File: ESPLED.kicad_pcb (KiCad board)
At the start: 2 copper layers, 81.3 x 83.8 mm, 24 parts, among them CON1 BARREL_JACK, J1 USB_B_Micro, P2 LED_CON, P3 LED_CON_SCREW, P4 LED_CON_SCREW, Q1 IRLZ34N, Q2 IRLZ34N, Q3 IRLZ34N, SW1 Reset, SW2 Program, U1 LM1117-3.3, U2 ESP-07v2, U3 INTERFACE-CH340G, Y1 Crystal

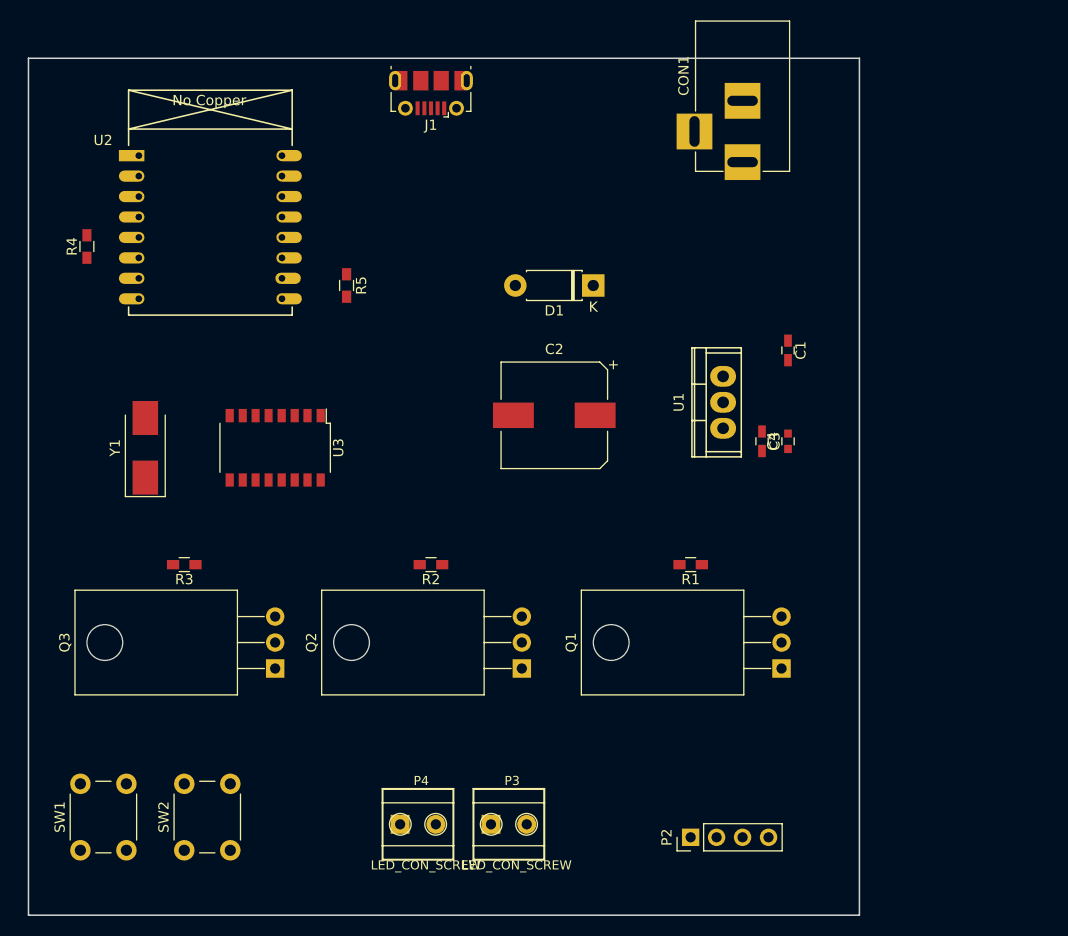
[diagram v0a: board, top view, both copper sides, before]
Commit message: Added caps for crystal
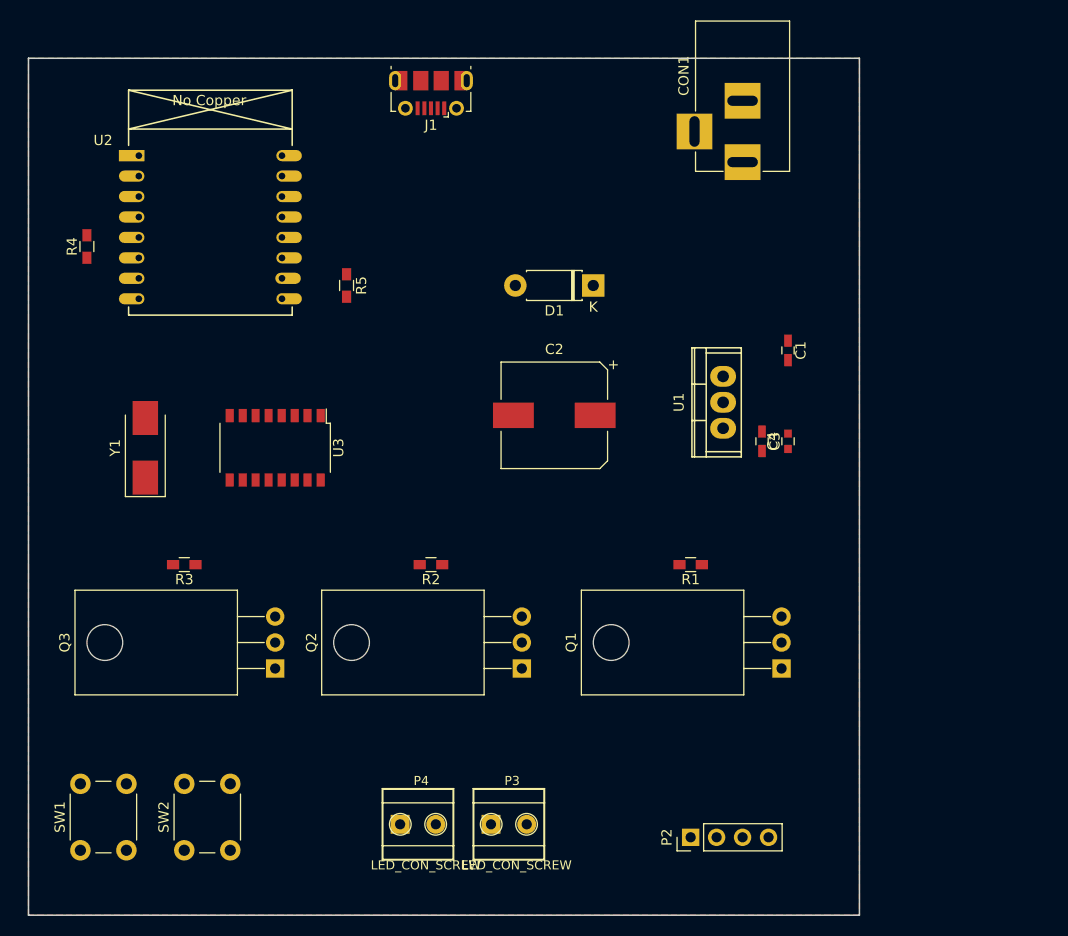
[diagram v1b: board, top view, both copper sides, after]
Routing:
- added copper zone on F.Cu, net GND
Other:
- net class High Power added: clearance 0.2, trace_width 0.25, via_dia 0.6, via_drill 0.4
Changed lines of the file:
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@@
     (links 62)
     (no_connects 60)
-    (area 0 0 0 0)
+    (area 92.634999 41.654999 174.065001 129.615001)
     (thickness 1.6)
-    (drawings 4)
+    (drawings 5)
     (tracks 0)
     (zones 0)
@@
     (add_net VUSB)
   )
+  (net_class "High Power" ""
+    (clearance 0.2)
+    (trace_width 0.25)
+    (via_dia 0.6)
+    (via_drill 0.4)
+    (uvia_dia 0.3)
+    (uvia_drill 0.1)
+  )
   (module Connectors:BARREL_JACK (layer F.Cu)
     (at 162.56 55.88 270)
@@
     )
   )
+  (dimension 83.82 (width 0.3) (layer Eco1.User)
+    (gr_text "83,820 mm" (at 189.31 87.63 270) (layer Eco1.User)
+      (effects (font (size 1.5 1.5) (thickness 0.3)))
+    )
+    (feature1 (pts (xy 179.07 129.54) (xy 190.66 129.54)))
+    (feature2 (pts (xy 179.07 45.72) (xy 190.66 45.72)))
+    (crossbar (pts (xy 187.96 45.72) (xy 187.96 129.54)))
+    (arrow1a (pts (xy 187.96 129.54) (xy 187.373579 128.413496)))
+    (arrow1b (pts (xy 187.96 129.54) (xy 188.546421 128.413496)))
+    (arrow2a (pts (xy 187.96 45.72) (xy 187.373579 46.846504)))
+    (arrow2b (pts (xy 187.96 45.72) (xy 188.546421 46.846504)))
+  )
   (gr_line (start 92.71 45.72) (end 173.99 45.72) (angle 90) (layer Edge.Cuts) (width 0.15))
   (gr_line (start 92.71 129.54) (end 92.71 45.72) (angle 90) (layer Edge.Cuts) (width 0.15))
   (gr_line (start 173.99 129.54) (end 92.71 129.54) (angle 90) (layer Edge.Cuts) (width 0.15))
   (gr_line (start 173.99 45.72) (end 173.99 129.54) (angle 90) (layer Edge.Cuts) (width 0.15))
+  (zone (net 2) (net_name GND) (layer F.Cu) (hatch edge 0.508)
+    (connect_pads (clearance 0.508))
+    (min_thickness 0.254)
+    (fill (arc_segments 16) (thermal_gap 0.508) (thermal_bridge_width 0.508))
+    (polygon
+      (pts
+        (xy 173.99 129.54) (xy 92.71 129.54) (xy 92.71 45.72) (xy 173.99 45.72)
+      )
+    )
+  )
 )

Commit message: Footprint research done, layout more or less gelayoutet
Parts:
- removed P4: LED_CON_SCREW, SeeedOPL-Connector:H2-3.5-7.0X7.0MM
- added C5: 22p, Capacitor_SMD:C_0603_1608Metric_Pad1.05x0.95mm_HandSolder, F.Cu at (112.9, 86.5)
- added C6: 22p, Capacitor_SMD:C_0603_1608Metric_Pad1.05x0.95mm_HandSolder, F.Cu at (112.9, 78.5)
- added C7: 100n, Capacitor_SMD:C_0603_1608Metric_Pad1.05x0.95mm_HandSolder, F.Cu at (133.0, 86.0)
- added F1: Polyfuse, Fuse:Fuse_1812_4532Metric_Pad1.30x3.40mm_HandSolder, F.Cu at (103.0, 69.7)
- added J2: LED_CON_RGB, Connector_PinHeader_2.54mm:PinHeader_1x04_P2.54mm_Vertical, F.Cu at (190.0, 111.0)
- added J3: LED_CON_WW, Connector_PinHeader_2.54mm:PinHeader_1x02_P2.54mm_Vertical, F.Cu at (185.0, 106.0)
- added J4: MIC, Connector_PinHeader_2.54mm:PinHeader_1x03_P2.54mm_Vertical, F.Cu at (145.0, 83.0)
- added JP1: GPIO LINK, Jumper:SolderJumper-2_P1.3mm_Open_RoundedPad1.0x1.5mm, F.Cu at (144.6, 90.5)
- added JP2: GPIO LINK, Jumper:SolderJumper-2_P1.3mm_Open_RoundedPad1.0x1.5mm, F.Cu at (107.4, 90.8)
- added JP3: GPIO LINK, Jumper:SolderJumper-2_P1.3mm_Open_RoundedPad1.0x1.5mm, F.Cu at (132.2, 90.7)
- added JP4: GND LINK, Jumper:SolderJumper-2_P1.3mm_Open_TrianglePad1.0x1.5mm, F.Cu at (98.2, 90.8)
- added JP5: GPIO LINK, Jumper:SolderJumper-2_P1.3mm_Open_RoundedPad1.0x1.5mm, F.Cu at (119.8, 90.5)
- added JP6: GPIO LINK, Jumper:SolderJumper-2_P1.3mm_Open_RoundedPad1.0x1.5mm, F.Cu at (95.0, 90.8)
- added P1: LED_CON_SCREW, TerminalBlock:TerminalBlock_Altech_AK300-2_P5.00mm, F.Cu at (186.0, 74.0)
- added Q4: IRLZ34N, Package_TO_SOT_THT:TO-220-3_Horizontal_TabDown, F.Cu at (113.4, 94.4)
- added Q5: IRLZ34N, Package_TO_SOT_THT:TO-220-3_Horizontal_TabDown, F.Cu at (100.9, 94.5)
- added R6: 100, Resistor_SMD:R_0603_1608Metric_Pad1.05x0.95mm_HandSolder, F.Cu at (113.6, 90.8)
- added R7: 100, Resistor_SMD:R_0603_1608Metric_Pad1.05x0.95mm_HandSolder, F.Cu at (101.2, 90.8)
- added R8: 4.7K, Resistor_SMD:R_0603_1608Metric_Pad1.05x0.95mm_HandSolder, F.Cu at (132.0, 83.0)
- added SW3: Mode, Button_Switch_THT:SW_PUSH_6mm, F.Cu at (174.0, 113.0)
- added U4: DS18B20, Package_TO_SOT_THT:TO-92_HandSolder, F.Cu at (136.9, 81.8)
- C1, C3: footprint Capacitors_SMD:C_0603_HandSoldering -> Capacitor_SMD:C_0603_1608Metric_Pad1.05x0.95mm_HandSolder
- C2: footprint Capacitors_SMD:CP_Elec_10x10.5 -> Capacitor_SMD:CP_Elec_10x10.5
- C4: footprint Capacitors_SMD:C_0603 -> Capacitor_SMD:C_0603_1608Metric_Pad1.05x0.95mm_HandSolder
- CON1: footprint Connectors:BARREL_JACK -> Connector_BarrelJack:BarrelJack_Horizontal
- D1: value 1N5819 -> 1N5817; footprint Diode_THT:D_DO-41_SOD81_P7.62mm_Horizontal -> Diode_SMD:D_SMA_Handsoldering
- J1: footprint Connectors_USB:USB_Micro-B_Molex-105017-0001 -> Connector_USB:USB_Micro-B_Molex-105017-0001
- P2: value LED_CON -> LED_CON_SCREW; footprint Pin_Headers:Pin_Header_Straight_1x04_Pitch2.54mm -> TerminalBlock:TerminalBlock_Altech_AK300-2_P5.00mm
- P3: footprint SeeedOPL-Connector:H2-3.5-7.0X7.0MM -> TerminalBlock:TerminalBlock_Altech_AK300-2_P5.00mm
- Q1, Q2, Q3: footprint TO_SOT_Packages_THT:TO-220_Horizontal -> Package_TO_SOT_THT:TO-220-3_Horizontal_TabDown
- R1, R2, R3, R4, R5: footprint Resistors_SMD:R_0603_HandSoldering -> Resistor_SMD:R_0603_1608Metric_Pad1.05x0.95mm_HandSolder
- SW1: footprint Buttons_Switches_THT:SW_PUSH_6mm_h5mm -> Button_Switch_THT:SW_PUSH_6mm
- SW2: footprint Button_Switch_THT:SW_PUSH_6mm_H5mm -> Button_Switch_THT:SW_PUSH_6mm
- U1: value LM1117-3.3 -> AMS1117-3.3; footprint Power_Integrations:TO-220 -> Package_TO_SOT_SMD:SOT-223-3_TabPin2
- U2: footprint ESP8266:ESP-07v2 -> RF_Module:ESP-07
- U3: footprint Housings_SSOP:SOP-16_4.4x10.4mm_Pitch1.27mm -> Package_SO:SOIC-16W_5.3x10.2mm_P1.27mm
- moved U2 67.1 mm to (167.0, 77.0)
- moved CON1 61.4 mm to (107.0, 82.0), turned to 0 degrees
- moved SW1 59.1 mm to (156.0, 113.0)
- moved R4 59.0 mm to (156.0, 77.1)
- moved SW2 58.0 mm to (165.0, 113.0)
- moved R5 56.8 mm to (178.0, 85.0)
- moved C3 56.2 mm to (110.0, 69.2), turned to 90 degrees
- moved P3 51.6 mm to (186.0, 98.0), turned to 90 degrees
- moved P2 45.9 mm to (186.0, 86.0)
- moved U1 45.1 mm to (116.4, 71.0), turned to 0 degrees
- moved C1 44.0 mm to (123.0, 74.9)
- moved D1 42.5 mm to (106.0, 75.0)
- moved J1 42.0 mm to (96.0, 69.7), turned to 270 degrees
- moved C4 31.4 mm to (136.0, 78.0), turned to 180 degrees
- moved Q1 18.9 mm to (150.8, 94.5), turned to 180 degrees
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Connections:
- D1 pad 2: VUSB -> Net-(D1-Pad2)
- P2 pad 1: Net-(P2-Pad1) -> Net-(J2-Pad1)
- P2 pad 2: Net-(P2-Pad2) -> Net-(J2-Pad2)
- P3 pad 1: Net-(P2-Pad3) -> Net-(J3-Pad1)
- P3 pad 2: +12V -> Net-(J3-Pad2)
- Q1 pad 2: Net-(P2-Pad1) -> Net-(J2-Pad3)
- Q2 pad 2: Net-(P2-Pad2) -> Net-(J2-Pad1)
- Q3 pad 2: Net-(P2-Pad3) -> Net-(J3-Pad1)
- R1 pad 2: Net-(R1-Pad2) -> Net-(JP1-Pad2)
- R2 pad 2: Net-(R2-Pad2) -> Net-(JP3-Pad2)
- R3 pad 2: Net-(R3-Pad2) -> Net-(JP5-Pad2)
- U2 pad 4: Net-(U2-Pad4) -> Net-(JP5-Pad2)
- U2 pad 5: Net-(R3-Pad2) -> Net-(JP3-Pad2)
- U2 pad 6: Net-(R2-Pad2) -> Net-(JP1-Pad2)
- U2 pad 7: Net-(R1-Pad2) -> Net-(JP2-Pad2)
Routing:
- removed copper zone on F.Cu, net GND
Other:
- board size 81.3 x 83.8 mm -> 100 x 50 mm

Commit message: Ongoin reordering. Will probably
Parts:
- moved JP6 50.0 mm to (145.0, 90.5)
- moved R7 50.0 mm to (151.2, 90.5)
- moved JP4 50.0 mm to (148.2, 90.5)
- moved Q5 50.0 mm to (150.9, 94.4)
- moved Q4 25.0 mm to (138.4, 94.4)
- moved R1 25.0 mm to (125.8, 90.5)
- moved R6 25.0 mm to (138.6, 90.5)
- moved JP2 25.0 mm to (132.4, 90.5)
- moved R2 25.0 mm to (113.4, 90.5)
- moved JP3 25.0 mm to (107.2, 90.5)
- moved JP1 25.0 mm to (119.6, 90.5)
- moved JP5 25.0 mm to (94.8, 90.5)
- moved Q3 25.0 mm to (100.9, 94.4)
- moved R3 25.0 mm to (101.0, 90.5)
- moved Q2 25.0 mm to (113.4, 94.4)
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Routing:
- net +3V3: track 0.00 -> 69.7 mm, vias 0 -> 1
- net TXD: track 0.00 -> 52.9 mm
- net RXD: track 0.00 -> 50.8 mm
- net Net-(R4-Pad2): track 0.00 -> 21.3 mm
- net Net-(J4-Pad1): track 0.00 -> 18.7 mm
- net +12V: track 0.00 -> 15.1 mm
- net Net-(C6-Pad1): track 0.00 -> 13.3 mm
- net Net-(C5-Pad1): track 0.00 -> 6.64 mm
- net VUSB: track 0.00 -> 5.92 mm
- net Net-(R8-Pad2): track 0.00 -> 4.16 mm
- net Net-(D1-Pad2): track 0.00 -> 3.24 mm
- added copper zone on F.Cu, net +3V3
- added copper zone on F.Cu, net GND
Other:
- net class Default: clearance 0.2 -> 0.1524; trace_width 0.25 -> 0.254; via_dia 0.6 -> 1; via_drill 0.4 -> 0.6
- net class High Power: clearance 0.2 -> 0.254; trace_width 0.25 -> 1.27; via_dia 0.6 -> 1.27; via_drill 0.4 -> 0.8
- net class Middle Power added: clearance 0.2032, trace_width 0.635, via_dia 1, via_drill 0.6
- rule trace_clearance: 0.2 -> 0.1524
- rule trace_min: 0.2 -> 0.1524
- rule via_min_drill: 0.3 -> 0.299999
- rule via_min_size: 0.4 -> 0.381

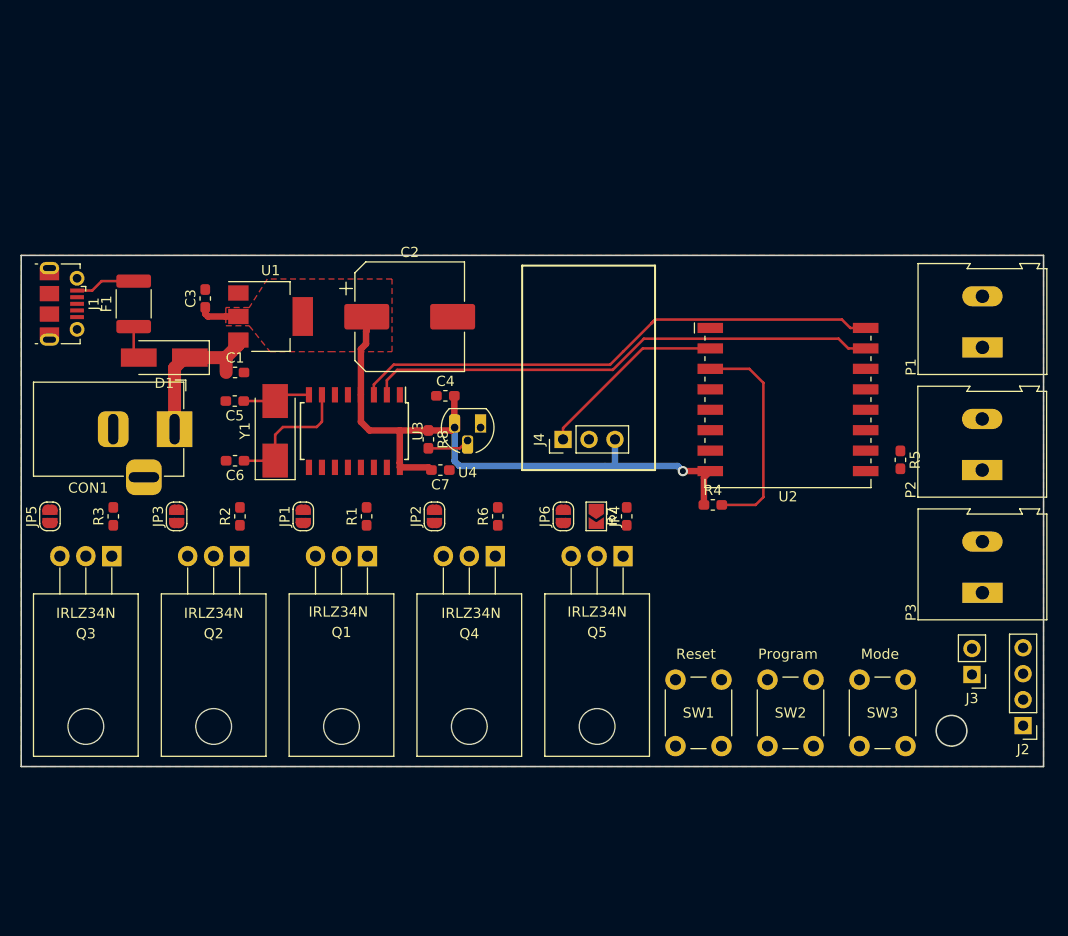
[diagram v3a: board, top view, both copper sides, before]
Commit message: Routing done! Next step: verification
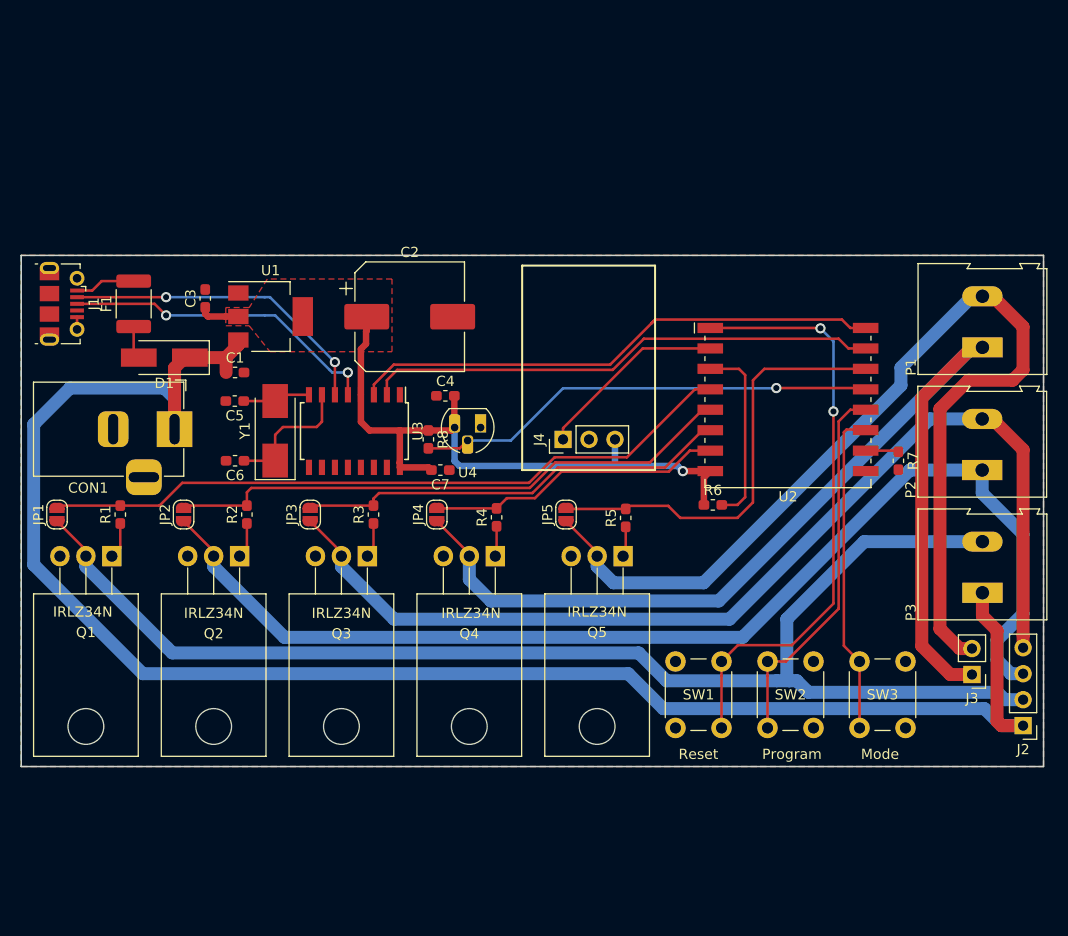
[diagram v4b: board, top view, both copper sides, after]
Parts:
- removed JP6: GPIO LINK, Jumper:SolderJumper-2_P1.3mm_Open_RoundedPad1.0x1.5mm
- JP4: value GND LINK -> GPIO LINK; footprint Jumper:SolderJumper-2_P1.3mm_Open_TrianglePad1.0x1.5mm -> Jumper:SolderJumper-2_P1.3mm_Open_RoundedPad1.0x1.5mm
- R4, R5: value 10k -> 100
- R6, R7: value 100 -> 10k
- moved JP5 50.5 mm to (145.3, 90.3)
- moved R5 27.5 mm to (151.1, 90.7), turned to 90 degrees
- moved R7 27.1 mm to (177.8, 85.1), turned to 270 degrees
- moved R3 25.5 mm to (126.5, 90.3)
- moved Q1 25.0 mm to (100.9, 94.4)
- moved Q3 25.0 mm to (125.9, 94.4)
- moved JP2 24.5 mm to (107.9, 90.3)
- moved R1 24.1 mm to (101.7, 90.3)
- moved JP1 24.1 mm to (95.5, 90.3)
- moved R4 21.2 mm to (138.5, 90.6), turned to 90 degrees
- moved R6 21.1 mm to (159.7, 89.4), turned to 0 degrees
- moved JP4 15.6 mm to (132.6, 90.3), turned to 90 degrees
- moved JP3 13.1 mm to (120.3, 90.3)
- moved SW1 1.78 mm to (156.0, 111.2)
- moved SW2 1.78 mm to (165.0, 111.2)
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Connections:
- J2 pad 1: Net-(J2-Pad1) -> +12V
- J2 pad 2: Net-(J2-Pad2) -> /CH1
- J2 pad 3: Net-(J2-Pad3) -> /CH2
- J2 pad 4: +12V -> /CH3
- J3 pad 1: Net-(J3-Pad1) -> /CH4
- J3 pad 2: Net-(J3-Pad2) -> /CH5
- JP1 pad 1: Net-(J2-Pad3) -> /CH1
- JP2 pad 1: Net-(J2-Pad2) -> /CH2
- JP3 pad 1: Net-(J2-Pad1) -> /CH3
- JP4 pad 1: GND -> /CH4
- JP4 pad 2: Net-(J3-Pad2) -> Net-(JP4-Pad2)
- JP5 pad 1: Net-(J3-Pad1) -> /CH5
- P1 pad 1: Net-(J2-Pad3) -> /CH4
- P1 pad 2: +12V -> /CH5
- P2 pad 1: Net-(J2-Pad1) -> /CH2
- P2 pad 2: Net-(J2-Pad2) -> /CH3
- P3 pad 1: Net-(J3-Pad1) -> +12V
- P3 pad 2: Net-(J3-Pad2) -> /CH1
- Q1 pad 2: Net-(J2-Pad3) -> /CH1
- Q2 pad 2: Net-(J2-Pad1) -> /CH2
- Q3 pad 2: Net-(J3-Pad1) -> /CH3
- Q4 pad 2: Net-(J2-Pad2) -> /CH4
- Q5 pad 2: Net-(J3-Pad2) -> /CH5
- R2 pad 2: Net-(JP3-Pad2) -> Net-(JP2-Pad2)
- R3 pad 2: Net-(JP5-Pad2) -> Net-(JP3-Pad2)
- R4 pad 1: +3V3 -> Net-(Q4-Pad1)
- R4 pad 2: Net-(R4-Pad2) -> Net-(JP4-Pad2)
- R5 pad 1: Net-(R5-Pad1) -> Net-(Q5-Pad1)
- R5 pad 2: GND -> Net-(JP5-Pad2)
- R6 pad 1: Net-(Q4-Pad1) -> +3V3
- R6 pad 2: Net-(JP2-Pad2) -> Net-(R6-Pad2)
- R7 pad 1: Net-(Q5-Pad1) -> Net-(R7-Pad1)
- R7 pad 2: Net-(JP6-Pad2) -> GND
- U2 pad 10: Net-(R5-Pad1) -> Net-(R7-Pad1)
- U2 pad 14: Net-(JP6-Pad2) -> Net-(JP5-Pad2)
- U2 pad 3: Net-(R4-Pad2) -> Net-(R6-Pad2)
- U2 pad 4: Net-(JP5-Pad2) -> Net-(JP1-Pad2)
- U2 pad 5: Net-(JP3-Pad2) -> Net-(JP2-Pad2)
- U2 pad 6: Net-(JP1-Pad2) -> Net-(JP3-Pad2)
- U2 pad 7: Net-(JP2-Pad2) -> Net-(JP4-Pad2)
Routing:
- net +12V: track 15.1 -> 166.7 mm
- net /CH1: track 0.00 -> 131.1 mm
- net /CH2: track 0.00 -> 114.9 mm
- net /CH4: track 0.00 -> 106.7 mm
- net /CH3: track 0.00 -> 103.2 mm
- net /CH5: track 0.00 -> 101.4 mm
- net Net-(JP1-Pad2): track 0.00 -> 68.7 mm
- net Net-(SW1-Pad2): track 0.00 -> 58.0 mm, vias 0 -> 2
- net Net-(JP2-Pad2): track 0.00 -> 56.3 mm
- net Net-(JP5-Pad2): track 0.00 -> 43.0 mm
- net Net-(JP3-Pad2): track 0.00 -> 42.7 mm
- net Net-(R8-Pad2): track 4.16 -> 45.4 mm, vias 0 -> 1
- net Net-(SW2-Pad1): track 0.00 -> 37.1 mm
- net Net-(SW3-Pad1): track 0.00 -> 31.8 mm
- net Net-(J1-Pad3): track 0.00 -> 31.5 mm, vias 0 -> 2
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- added copper zone on B.Cu, net GND
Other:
- outline, holes or cut-outs redrawn

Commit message: layout finished. Adding logic level converter
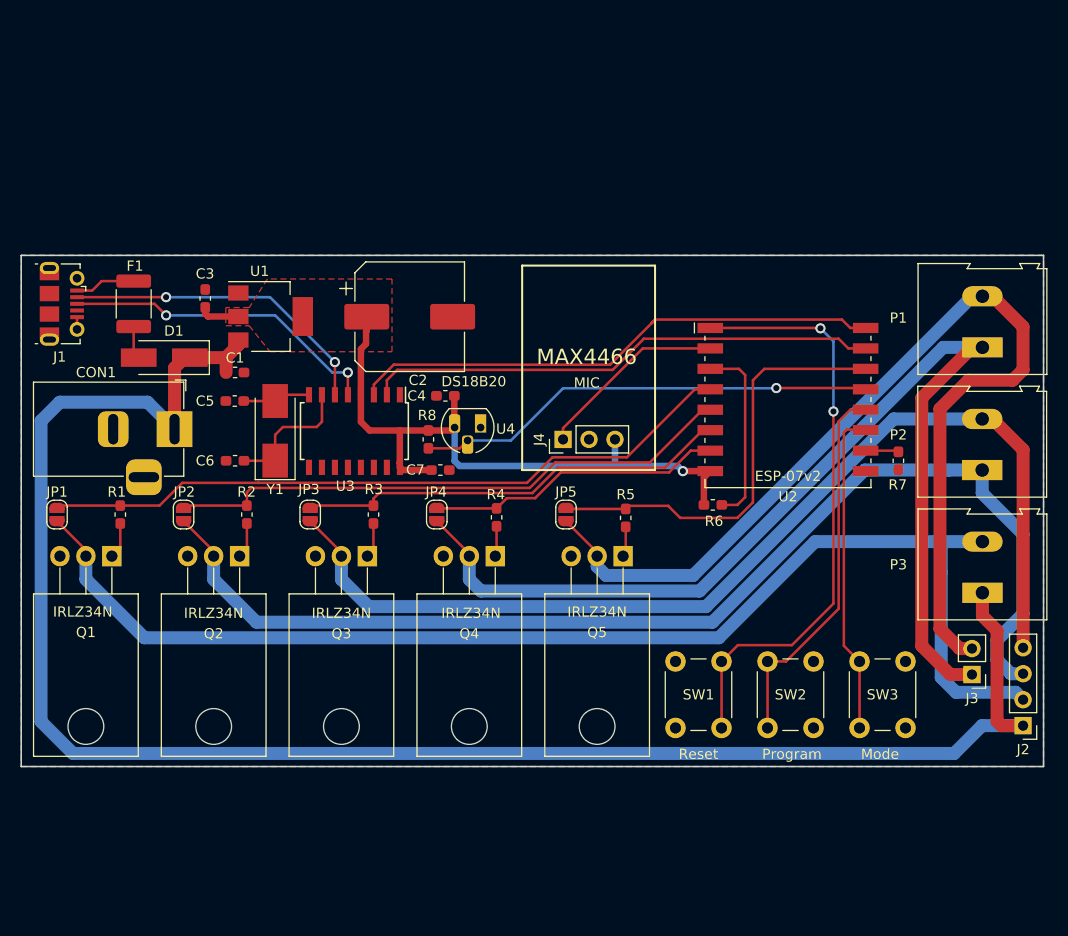
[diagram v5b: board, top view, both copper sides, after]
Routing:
- net /CH1: track 131.1 -> 123.0 mm
- net +12V: track 166.7 -> 173.8 mm
- net /CH5: track 101.4 -> 99.8 mm
- net /CH4: track 106.7 -> 105.9 mm
- net /CH3: track 103.2 -> 104.0 mm
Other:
- board text added: "MAX4466"
